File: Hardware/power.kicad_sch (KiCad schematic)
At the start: 21 parts, among them U3 LM66200DRLR, U4 MAX77827AEFD+T, U5 SC4215

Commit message: RAE logo
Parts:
- U5: value SC4215 -> SC4215ASTRT; symbol iclr:RT9025-25GSP -> iclr:SC4215ASTRT
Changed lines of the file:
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@@
 	)
 	(junction
+		(at 208.28 62.23)
+		(diameter 0)
+		(color 0 0 0 0)
+	)
+	(junction
 		(at 139.7 62.23)
 		(diameter 0)
@@
 	)
 	(junction
-		(at 207.01 62.23)
-		(diameter 0)
-		(color 0 0 0 0)
-	)
-	(junction
 		(at 246.38 62.23)
 		(diameter 0)
@@
 	)
 	(no_connect
-		(at 234.95 74.93)
+		(at 214.63 71.12)
 	)
 	(no_connect
-		(at 214.63 74.93)
+		(at 234.95 74.93)
 	)
 	(wire
@@
 	(wire
 		(pts
-			(xy 207.01 62.23) (xy 207.01 71.12)
-		)
-		(stroke
-			(width 0)
-			(type default)
-		)
-	)
-	(wire
-		(pts
 			(xy 172.72 62.23) (xy 185.42 62.23)
 		)
@@
 	(wire
 		(pts
+			(xy 208.28 67.31) (xy 208.28 62.23)
+		)
+		(stroke
+			(width 0)
+			(type default)
+		)
+	)
+	(wire
+		(pts
 			(xy 134.62 62.23) (xy 139.7 62.23)
 		)
@@
 	(wire
 		(pts
+			(xy 208.28 62.23) (xy 214.63 62.23)
+		)
+		(stroke
+			(width 0)
+			(type default)
+		)
+	)
+	(wire
+		(pts
 			(xy 246.38 68.58) (xy 246.38 71.12)
 		)
@@
 	(wire
 		(pts
-			(xy 200.66 62.23) (xy 207.01 62.23)
+			(xy 200.66 62.23) (xy 208.28 62.23)
 		)
 		(stroke
@@
 	(wire
 		(pts
-			(xy 207.01 62.23) (xy 214.63 62.23)
-		)
-		(stroke
-			(width 0)
-			(type default)
-		)
-	)
-	(wire
-		(pts
 			(xy 190.5 62.23) (xy 198.12 62.23)
 		)
@@
 	(wire
 		(pts
-			(xy 207.01 71.12) (xy 214.63 71.12)
+			(xy 138.43 77.47) (xy 142.24 77.47)
 		)
 		(stroke
@@
 	(wire
 		(pts
-			(xy 138.43 77.47) (xy 142.24 77.47)
+			(xy 214.63 67.31) (xy 208.28 67.31)
 		)
 		(stroke
@@
 	)
 	(symbol
-		(lib_id "iclr:RT9025-25GSP")
+		(lib_id "iclr:SC4215ASTRT")
 		(at 224.79 60.96 0)
 		(unit 1)
@@
 		(on_board yes)
 		(dnp no)
-		(fields_autoplaced yes)
 		(property "Reference" "U5"
-			(at 224.79 56.1172 0)
+			(at 224.79 54.61 0)
 			(effects
 				(font
@@
 			)
 		)
-		(property "Value" "SC4215"
-			(at 224.79 58.6541 0)
+		(property "Value" "SC4215ASTRT"
+			(at 224.79 57.15 0)
 			(effects
 				(font
@@
 		)
 		(property "Footprint" "iclr:SOIC127P599X175-9N"
-			(at 224.79 55.88 0)
+			(at 224.79 53.594 0)
 			(effects
 				(font
@@
 		(pin "9"
 		)
+		(pin "5"
+		)
 		(instances

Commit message: 30V compatibility update
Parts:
- L3: MPN (none) -> DFE201210U-1R0M
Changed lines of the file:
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@@
+			)
+		)
+		(property "MPN" "DFE201210U-1R0M"
+			(at 177.8 71.12 0)
+			(effects
+				(font
+					(size 1.27 1.27)
+				)
+				(hide yes)
 			)
 		)

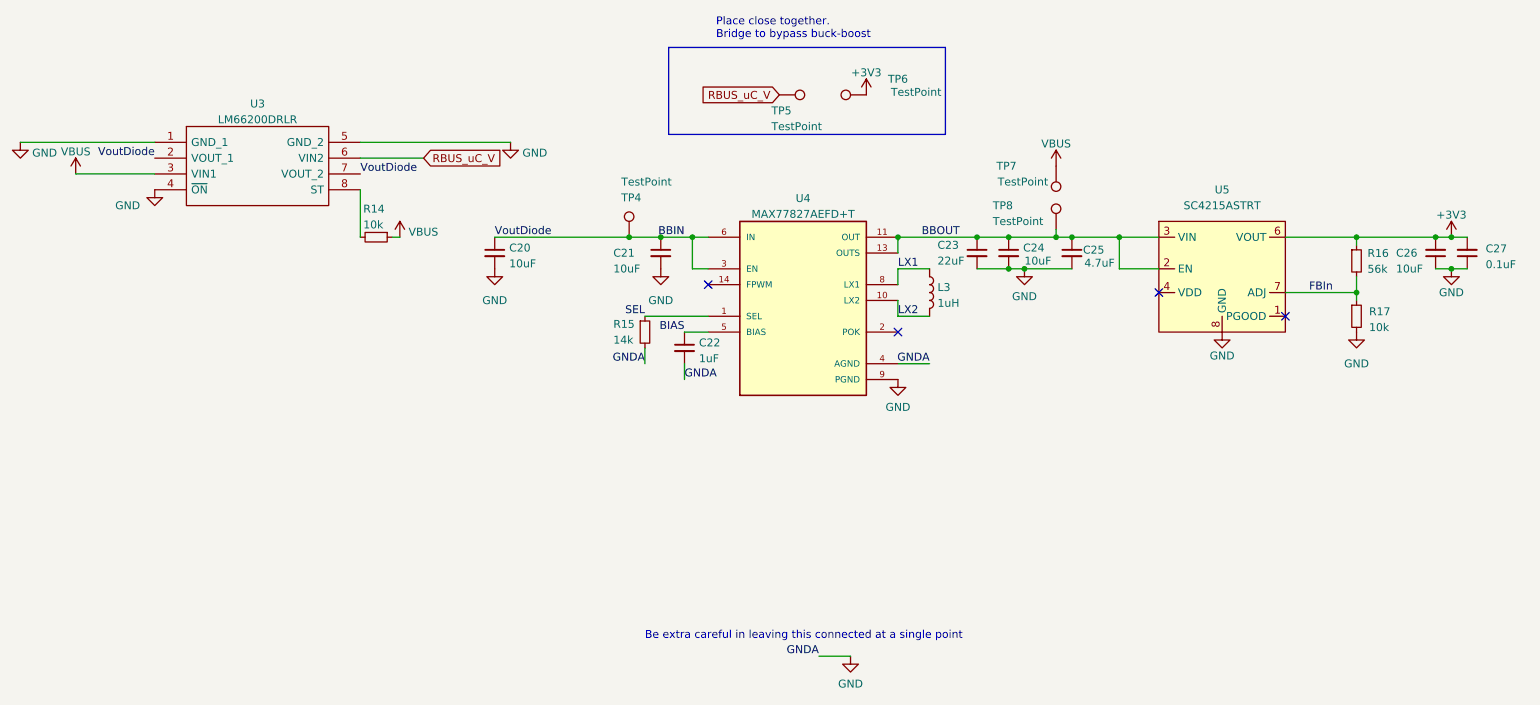
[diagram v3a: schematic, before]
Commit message: cleaned up schematic and bom
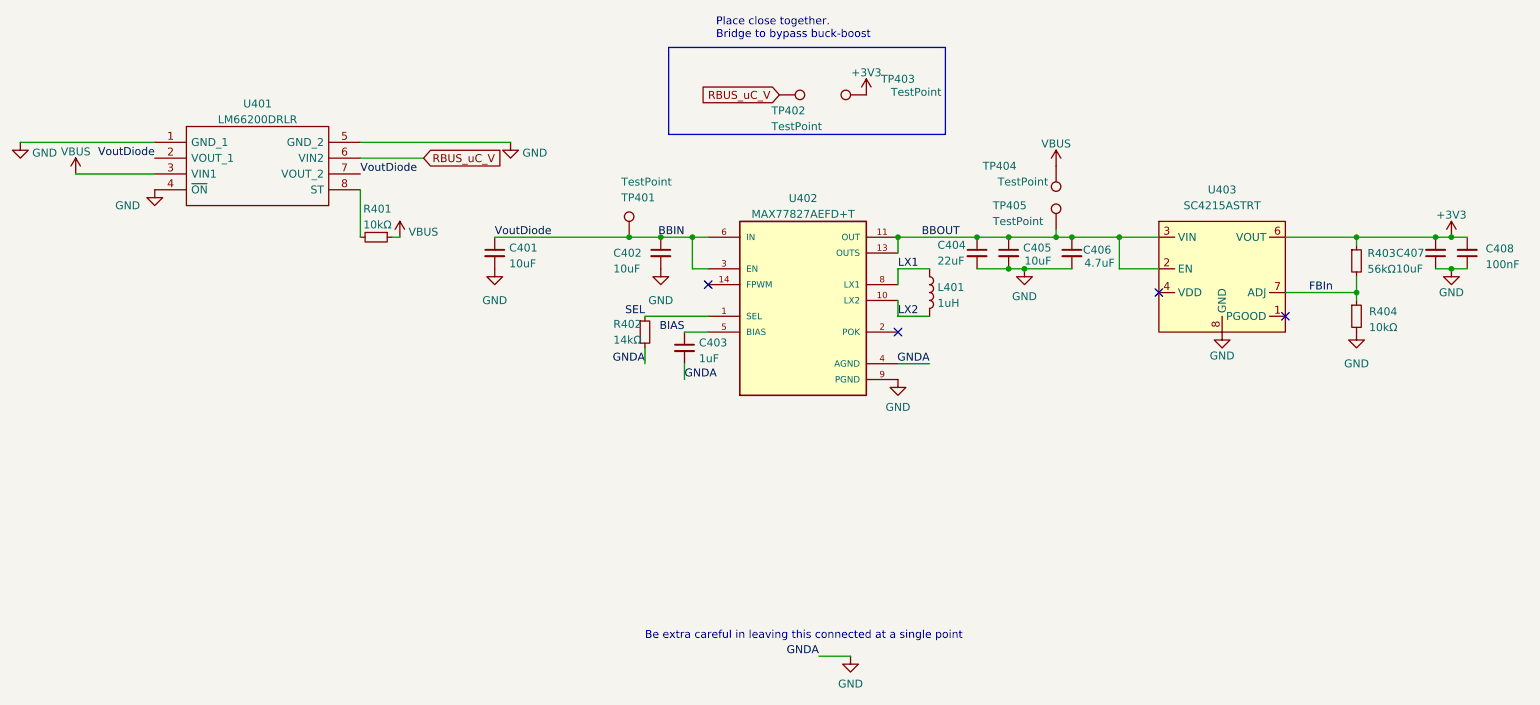
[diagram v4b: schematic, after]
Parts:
- C408: renamed from C27; value 0.1uF -> 100nF
- R401: renamed from R14; value 10k -> 10kΩ
- R402: renamed from R15; value 14k -> 14kΩ
- R403: renamed from R16; value 56k -> 56kΩ
- R404: renamed from R17; value 10k -> 10kΩ
- TP401: renamed from TP4; now left out of the parts list
- TP402: renamed from TP5; now left out of the parts list
- TP403: renamed from TP6; now left out of the parts list
- TP404: renamed from TP7; now left out of the parts list
- TP405: renamed from TP8; now left out of the parts list
- renumbered C20 to C401, C21 to C402, C22 to C403, C23 to C404, C24 to C405, C25 to C406, C26 to C407, L3 to L401, U3 to U401, U4 to U402, U5 to U403
